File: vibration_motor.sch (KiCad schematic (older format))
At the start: 4 parts, among them U3 ECH8693R-TL-W, U4 C0720B001F

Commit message: More PCB setup
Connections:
- net labels added: (GND)
- net labels removed: GND
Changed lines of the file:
@@
 EESchema Schematic File Version 4
 LIBS:nrf-cache
-EELAYER 26 0
+EELAYER 29 0
 EELAYER END
 $Descr A4 11693 8268
@@
 Text GLabel 4550 3650 0    50   Input ~ 0
 MOTOR_PWM
-$Comp
-L power:GND #PWR0108
-U 1 1 5D05CFA3
-P 4850 4850
-F 0 "#PWR0108" H 4850 4600 50  0001 C CNN
-F 1 "GND" H 4855 4677 50  0000 C CNN
-F 2 "" H 4850 4850 50  0001 C CNN
-F 3 "" H 4850 4850 50  0001 C CNN
-	1    4850 4850
-	1    0    0    -1
-$EndComp
 Wire Wire Line
 	6650 3400 6650 4250
@@
 	5350 4550 4850 4550
 Wire Wire Line
-	4850 4550 4850 4850
-Wire Wire Line
 	5350 4250 4850 4250
 Wire Wire Line
 	4850 4250 4850 4550
-Connection ~ 4850 4550
 Wire Wire Line
 	4550 3650 4850 3650
@@
 	1    0    0    -1
 $EndComp
+$Comp
+L power:(GND) #PWR?
+U 1 1 5D11D46A
+P 4850 4850
+F 0 "#PWR?" H 4850 4850 30  0001 C CNN
+F 1 "(GND)" H 4850 4850 30  0001 C CNN
+F 2 "" H 4850 4850 60  0000 C CNN
+F 3 "" H 4850 4850 60  0000 C CNN
+	1    4850 4850
+	1    0    0    -1
+$EndComp
+Connection ~ 4850 4550
+Wire Wire Line
+	4850 4550 4850 4850
 $EndSCHEMATC

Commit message: New PCB's
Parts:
- added J3: Conn_01x03, Pin_Headers:Pin_Header_Straight_1x03_Pitch2.54mm, symbol Connector_Generic:Conn_01x03
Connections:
- net (GND): now also J3.1 (Pin_1)
- net +3.3: now also J3.3 (Pin_3)
- net MOTOR_PWM: now also J3.2 (Pin_2)
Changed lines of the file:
@@
 $EndComp
 $Comp
-L power:(GND) #PWR?
+L power:(GND) #PWR0101
 U 1 1 5D11D46A
 P 4850 4850
-F 0 "#PWR?" H 4850 4850 30  0001 C CNN
+F 0 "#PWR0101" H 4850 4850 30  0001 C CNN
 F 1 "(GND)" H 4850 4850 30  0001 C CNN
 F 2 "" H 4850 4850 60  0000 C CNN
@@
 Wire Wire Line
 	4850 4550 4850 4850
+$Comp
+L Connector_Generic:Conn_01x03 J3
+U 1 1 5D1C2F7F
+P 7150 3750
+F 0 "J3" H 7068 3425 50  0000 C CNN
+F 1 "Conn_01x03" H 7068 3516 50  0000 C CNN
+F 2 "Pin_Headers:Pin_Header_Straight_1x03_Pitch2.54mm" H 7150 3750 50  0001 C CNN
+F 3 "~" H 7150 3750 50  0001 C CNN
+	1    7150 3750
+	-1   0    0    1
+$EndComp
+$Comp
+L power:(GND) #PWR0102
+U 1 1 5D1C3923
+P 7550 4000
+F 0 "#PWR0102" H 7550 4000 30  0001 C CNN
+F 1 "(GND)" H 7550 4000 30  0001 C CNN
+F 2 "" H 7550 4000 60  0000 C CNN
+F 3 "" H 7550 4000 60  0000 C CNN
+	1    7550 4000
+	1    0    0    -1
+$EndComp
+Wire Wire Line
+	7350 3850 7550 3850
+Wire Wire Line
+	7550 3850 7550 4000
+$Comp
+L power:+3.3 #PWR0103
+U 1 1 5D1C58C1
+P 7550 3350
+F 0 "#PWR0103" H 7550 3400 30  0001 C CNN
+F 1 "+3.3" H 7550 3483 50  0000 C CNN
+F 2 "" H 7550 3350 60  0000 C CNN
+F 3 "" H 7550 3350 60  0000 C CNN
+	1    7550 3350
+	1    0    0    -1
+$EndComp
+Wire Wire Line
+	7350 3650 7550 3650
+Wire Wire Line
+	7550 3650 7550 3350
+Text GLabel 7650 3750 2    50   Input ~ 0
+MOTOR_PWM
+Wire Wire Line
+	7350 3750 7650 3750
 $EndSCHEMATC

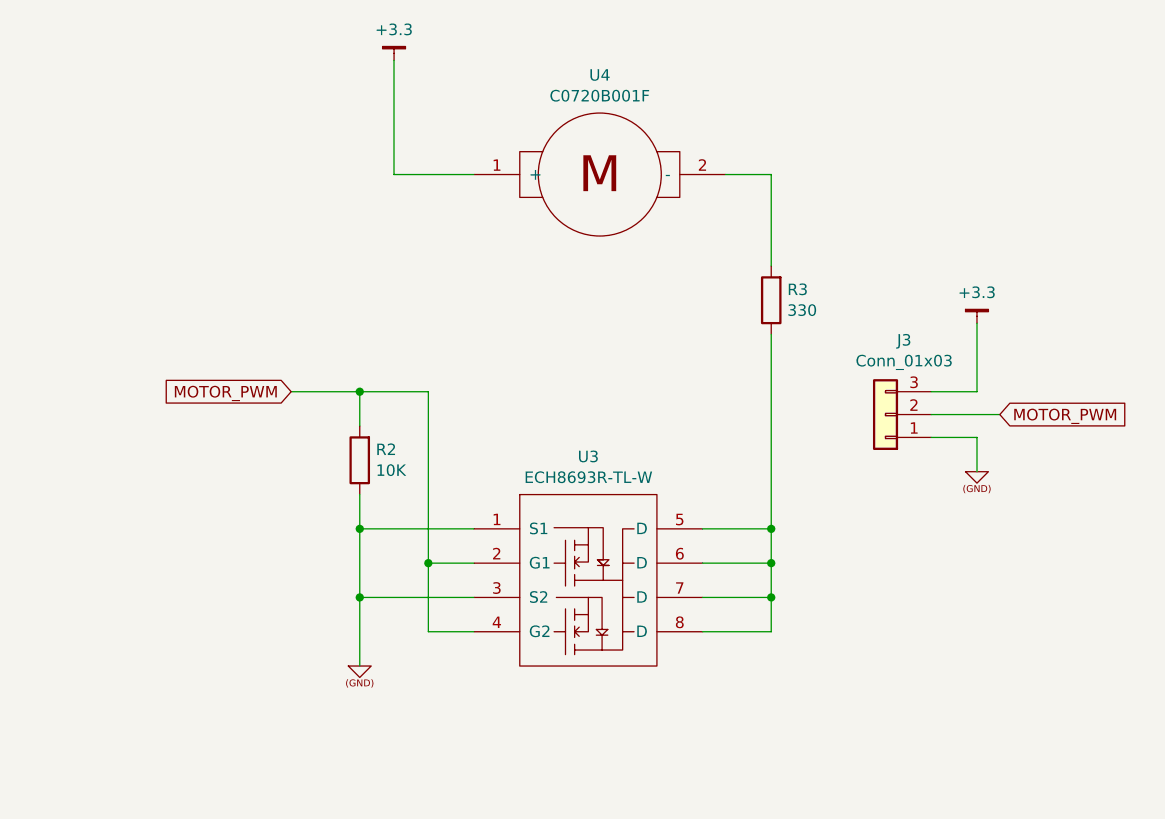
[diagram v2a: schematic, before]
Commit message: Rework and rename parts
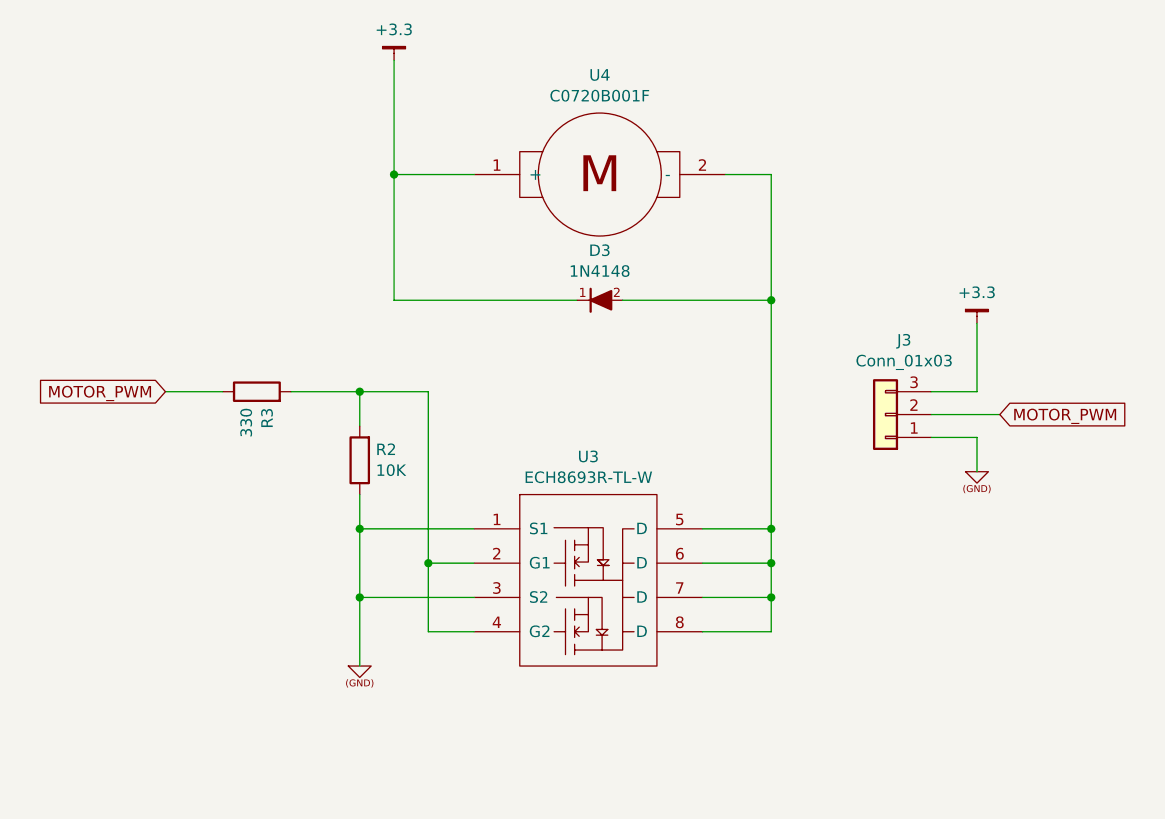
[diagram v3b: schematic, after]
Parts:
- added D3: 1N4148, Diodes_SMD:D_SOD-123, symbol _semi:DIODE
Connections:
- net +3.3: now also D3.1 (K)
- net MOTOR_PWM: now also R3.1; no longer R2.2, U3.2 (G1), U3.4 (G2)
- net at U4.2 (-): now also U3.5 (D), U3.6 (D), U3.7 (D), U3.8 (D), D3.2 (A); no longer R3.2
- new net: R2.2, R3.2, U3.2 (G1), U3.4 (G2)
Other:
- moved on the sheet: R3
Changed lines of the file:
@@
 EESchema Schematic File Version 4
-LIBS:nrf-cache
 EELAYER 29 0
 EELAYER END
 $Descr A4 11693 8268
 encoding utf-8
-Sheet 2 4
+Sheet 1 1
 Title ""
 Date ""
@@
 L Device:R R3
 U 1 1 5D05C2F6
-P 6650 3250
-F 0 "R3" H 6580 3204 50  0000 R CNN
-F 1 "330" H 6580 3295 50  0000 R CNN
-F 2 "Resistors_SMD:R_0805" V 6580 3250 50  0001 C CNN
-F 3 "~" H 6650 3250 50  0001 C CNN
-	1    6650 3250
-	-1   0    0    1
+P 4400 3650
+F 0 "R3" H 4330 3604 50  0000 R CNN
+F 1 "330" H 4330 3695 50  0000 R CNN
+F 2 "Resistors_SMD:R_0805" V 4330 3650 50  0001 C CNN
+F 3 "~" H 4400 3650 50  0001 C CNN
+	1    4400 3650
+	0    -1   -1   0
 $EndComp
 Wire Wire Line
 	6450 2700 6650 2700
-Wire Wire Line
-	6650 2700 6650 3100
-Text GLabel 4550 3650 0    50   Input ~ 0
+Text GLabel 4000 3650 0    50   Input ~ 0
 MOTOR_PWM
-Wire Wire Line
-	6650 3400 6650 4250
 Wire Wire Line
 	6650 4250 6350 4250
@@
 Wire Wire Line
 	4850 4250 4850 4550
-Wire Wire Line
-	4550 3650 4850 3650
 Wire Wire Line
 	5150 3650 5150 4400
@@
 Wire Wire Line
 	4850 3650 4850 3800
-Connection ~ 4850 3650
 Wire Wire Line
 	4850 3650 5150 3650
@@
 Wire Wire Line
 	7350 3750 7650 3750
+Connection ~ 5000 2700
+$Comp
+L _semi:DIODE D3
+U 1 1 5D47650F
+P 5900 3250
+F 0 "D3" V 5683 3250 50  0000 C CNN
+F 1 "1N4148" V 5774 3250 50  0000 C CNN
+F 2 "Diodes_SMD:D_SOD-123" H 5900 3250 60  0001 C CNN
+F 3 "" H 5900 3250 60  0000 C CNN
+	1    5900 3250
+	0    1    1    0
+$EndComp
+Wire Wire Line
+	6000 3250 6650 3250
+Connection ~ 6650 3250
+Wire Wire Line
+	6650 3250 6650 4250
+Wire Wire Line
+	5800 3250 5000 3250
+Wire Wire Line
+	6650 2700 6650 3250
+Wire Wire Line
+	5000 2700 5000 3250
+Wire Wire Line
+	4000 3650 4250 3650
+Wire Wire Line
+	4550 3650 4850 3650
+Connection ~ 4850 3650
 $EndSCHEMATC

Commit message: Power board PCB
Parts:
- D3: value 1N4148 -> ZLLS410; footprint Diodes_SMD:D_SOD-123 -> Diodes_SMD:D_SOD-323
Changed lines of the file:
@@
 P 5900 3250
 F 0 "D3" V 5683 3250 50  0000 C CNN
-F 1 "1N4148" V 5774 3250 50  0000 C CNN
-F 2 "Diodes_SMD:D_SOD-123" H 5900 3250 60  0001 C CNN
+F 1 "ZLLS410" V 5774 3250 50  0000 C CNN
+F 2 "Diodes_SMD:D_SOD-323" H 5900 3250 60  0001 C CNN
 F 3 "" H 5900 3250 60  0000 C CNN
 	1    5900 3250
